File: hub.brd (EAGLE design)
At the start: 160 x 100 mm, 27 parts, among them U1 10118194-MICRO-USB, U2 LM3671MF-3.3/NOPBMF05A-M, U3 SN74LVC1T45DBVRDBV6-M, U4 SN74LVC1T45DBVRDBV6-M

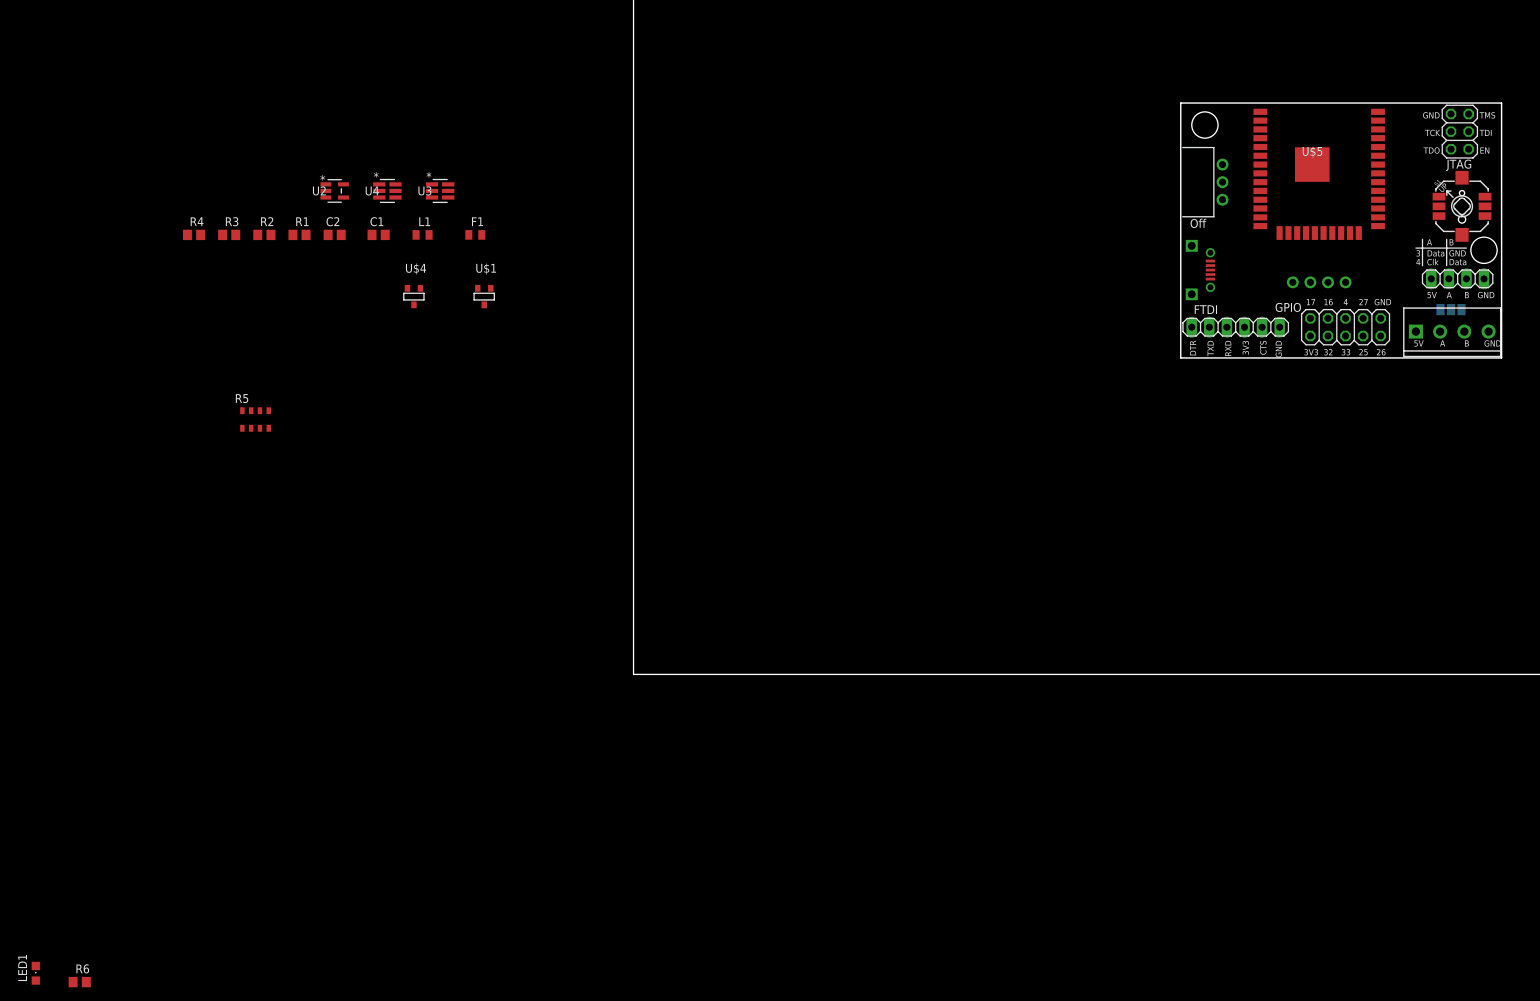
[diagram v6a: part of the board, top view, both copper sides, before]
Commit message: Finished placing components and started laying out traces
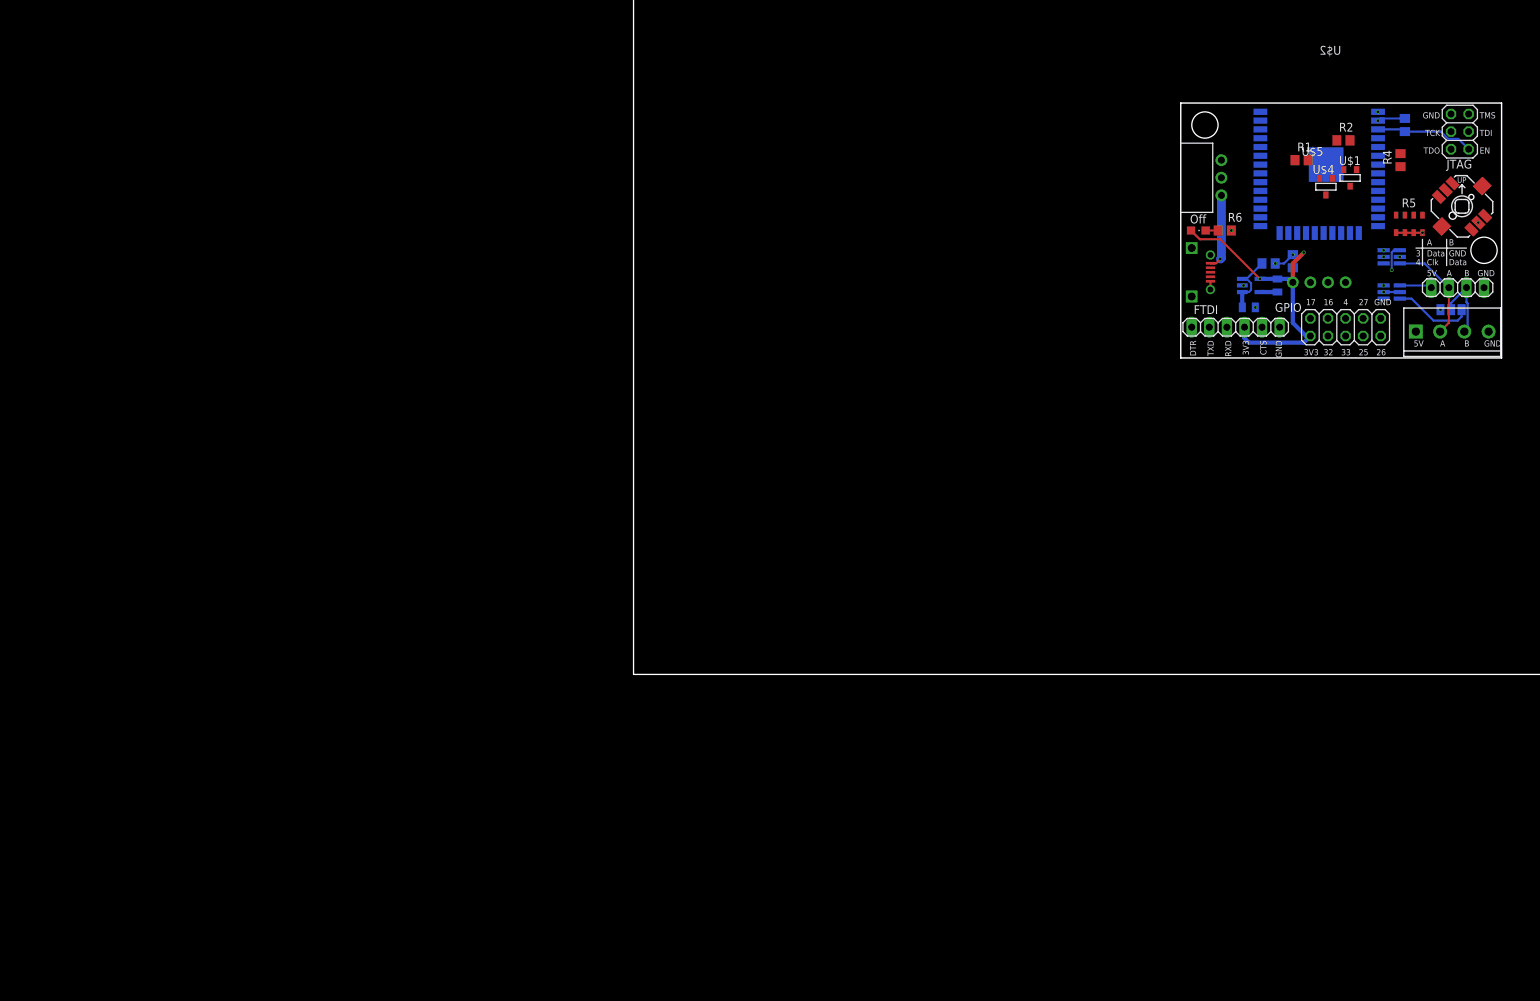
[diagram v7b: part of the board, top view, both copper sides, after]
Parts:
- moved LED1 199.3 mm to (81.6, 64.1), turned to 270 degrees
- moved R6 197.9 mm to (85.4, 64.1), turned to 180 degrees
- moved R4 174.6 mm to (110.8, 74.3), turned to 90 degrees
- moved R3 170.6 mm to (111.4, 79.4), flipped to the bottom, turned to 90 degrees
- moved R5 169.1 mm to (112.1, 65.1)
- moved R2 156.5 mm to (102.6, 77.2)
- moved U4 145.4 mm to (109.5, 60.3), flipped to the bottom
- moved R1 145.2 mm to (96.5, 74.3)
- moved C2 138.5 mm to (95.2, 59.7), flipped to the bottom, turned to 90 degrees
- moved U3 138.3 mm to (109.5, 55.2), flipped to the bottom
- moved U2 133.1 mm to (89.2, 56.2), flipped to the bottom, turned to 180 degrees
- moved U$4 132.7 mm to (100.0, 70.5)
- moved C1 128.7 mm to (91.8, 59.4), flipped to the bottom, turned to 180 degrees
- moved U$1 126.3 mm to (103.5, 71.8)
- moved L1 123.7 mm to (93.0, 56.2), flipped to the bottom, turned to 90 degrees
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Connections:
- net +5V: now also U$3.2
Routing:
- net VCC: track 0.00 -> 53.6 mm, vias 0 -> 6
- net N$9: track 0.00 -> 15.4 mm
- net EN: track 0.00 -> 14.3 mm
- net N$8: track 0.00 -> 11.5 mm
- net N$2: track 0.00 -> 11.0 mm, vias 0 -> 1
- net N$7: track 0.00 -> 10.7 mm
- net N$3: track 0.00 -> 9.89 mm
- net +5V: track 0.00 -> 8.52 mm, vias 0 -> 2
- net GND: track 0.00 -> 6.79 mm, vias 0 -> 10
- net N$1: track 0.00 -> 2.55 mm
- net N$10: track 0.00 -> 1.81 mm
- added copper zone on layer 15, net +5V
- added copper zone on layer 2, net GND
- added copper zone on layer 15, net VCC

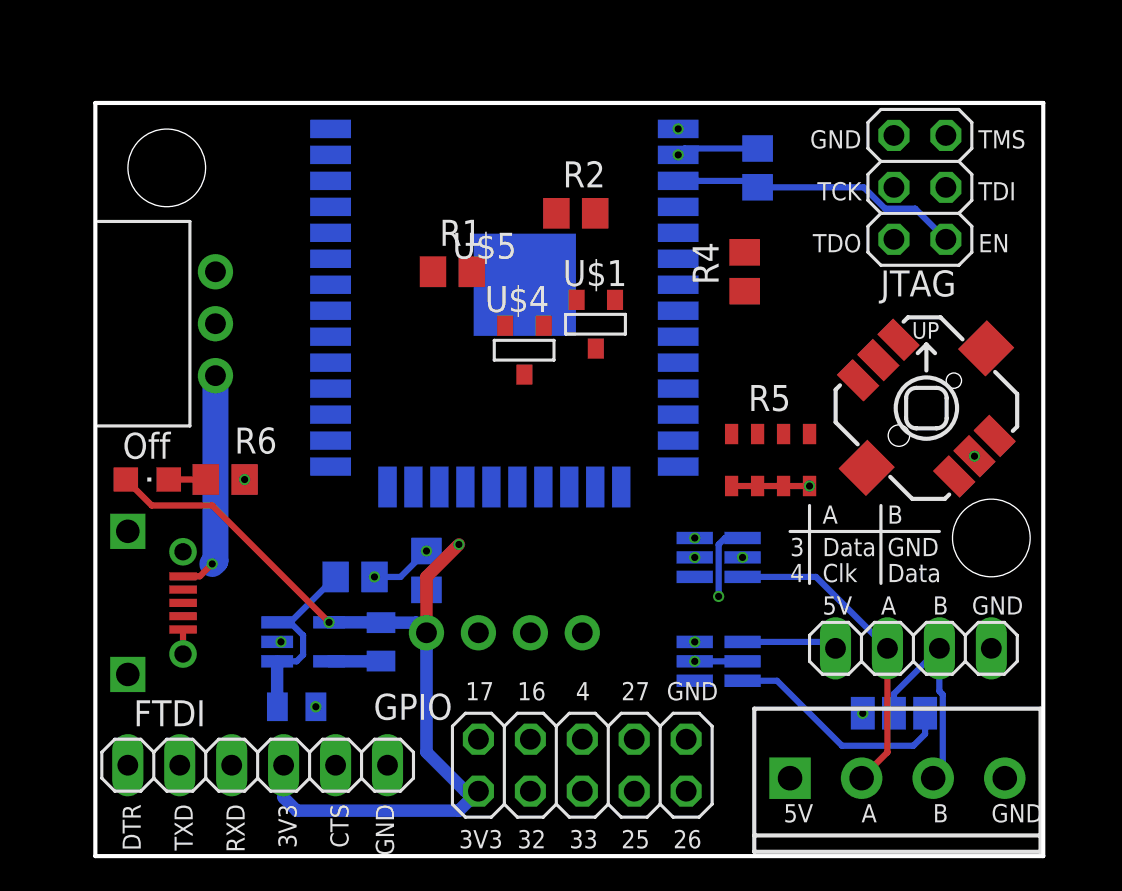
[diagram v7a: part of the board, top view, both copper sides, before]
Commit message: Wired up lots of support circuitry
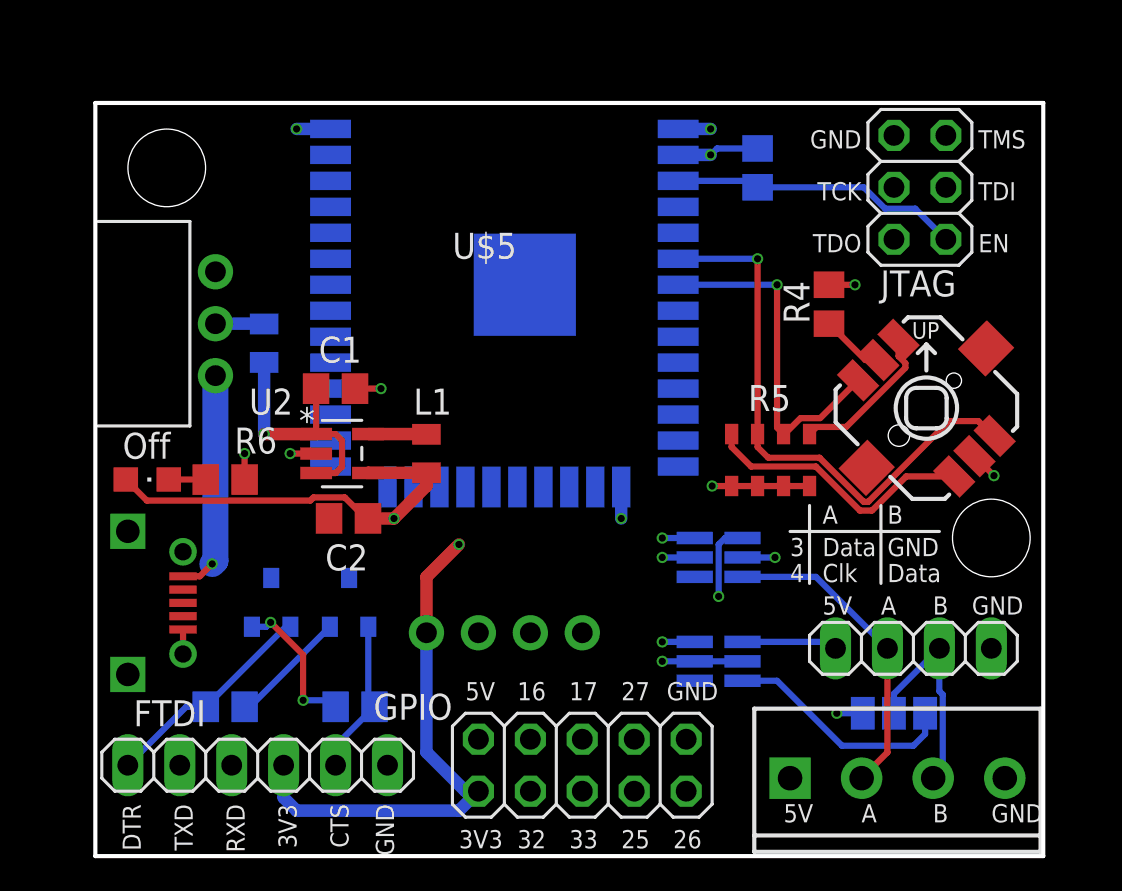
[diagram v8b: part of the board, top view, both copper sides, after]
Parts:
- moved R2 26.4 mm to (91.8, 53.0), flipped to the bottom, turned to 180 degrees
- moved R1 24.0 mm to (85.4, 53.0), flipped to the bottom
- moved U$1 18.2 mm to (91.4, 58.1), flipped to the bottom, turned to 180 degrees
- moved F1 17.9 mm to (87.3, 70.8), turned to 270 degrees
- moved U$4 17.5 mm to (87.6, 58.1), flipped to the bottom, turned to 180 degrees
- moved L1 9.47 mm to (95.2, 65.4), flipped to the top, turned to 270 degrees
- moved U2 9.40 mm to (91.1, 65.4), flipped to the top, turned to 0 degrees
- moved C1 9.26 mm to (90.8, 68.6), flipped to the top, turned to 0 degrees
- moved C2 4.58 mm to (91.4, 62.2), flipped to the top, turned to 180 degrees
- moved R4 4.42 mm to (114.9, 72.7)
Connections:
- removed net GPIO4: JP7.6, U$2.26
- net +5V: now also JP7.2
- net CENTER: now also U$2.26
- net DOWN: now also U$2.29
- net GPIO17: now also JP7.6; no longer JP7.2
- net LEFT: now also U$2.7
- net RIGHT: now also R5.P$2, U$2.6; no longer R5.P$4
- net UP: now also R5.P$4, U$2.31; no longer R5.P$2
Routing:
- net RIGHT: track 0.00 -> 27.7 mm, vias 0 -> 1
- net LEFT: track 0.00 -> 17.0 mm, vias 0 -> 1
- net DOWN: track 0.00 -> 13.5 mm
- net GND: track 6.79 -> 19.5 mm, vias 10 -> 11
- net N$12: track 0.00 -> 10.8 mm
- net N$6: track 0.00 -> 7.68 mm
- net UP: track 0.00 -> 7.54 mm
- net N$5: track 0.00 -> 7.19 mm, vias 0 -> 2
- net N$4: track 0.00 -> 5.79 mm
- net VCC: track 53.6 -> 58.9 mm, vias 6 -> 7
- net CENTER: track 0.00 -> 3.15 mm
- net N$3: track 9.89 -> 12.3 mm, vias 0 -> 1
- net +5V: track 8.52 -> 10.9 mm, vias 2 -> 1
